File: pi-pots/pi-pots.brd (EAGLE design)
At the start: 40.6 x 101.6 mm, 5 parts, among them J1 PINHD-3X4

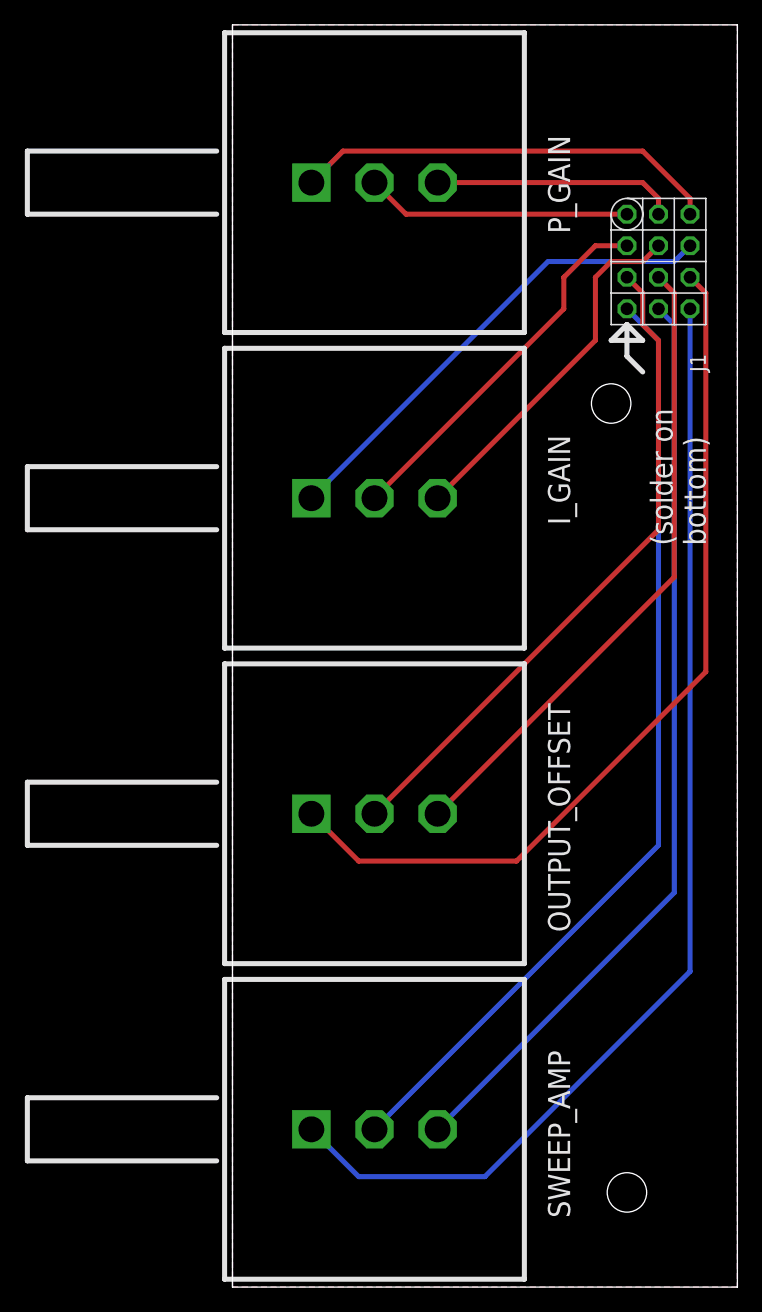
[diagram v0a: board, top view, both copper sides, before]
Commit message: Calibration Windows
I've opened up windows above POT1-3 and U9, pin 10. The windows allow access to the pots and U9 for initial calibration of the PI controller.

DSB
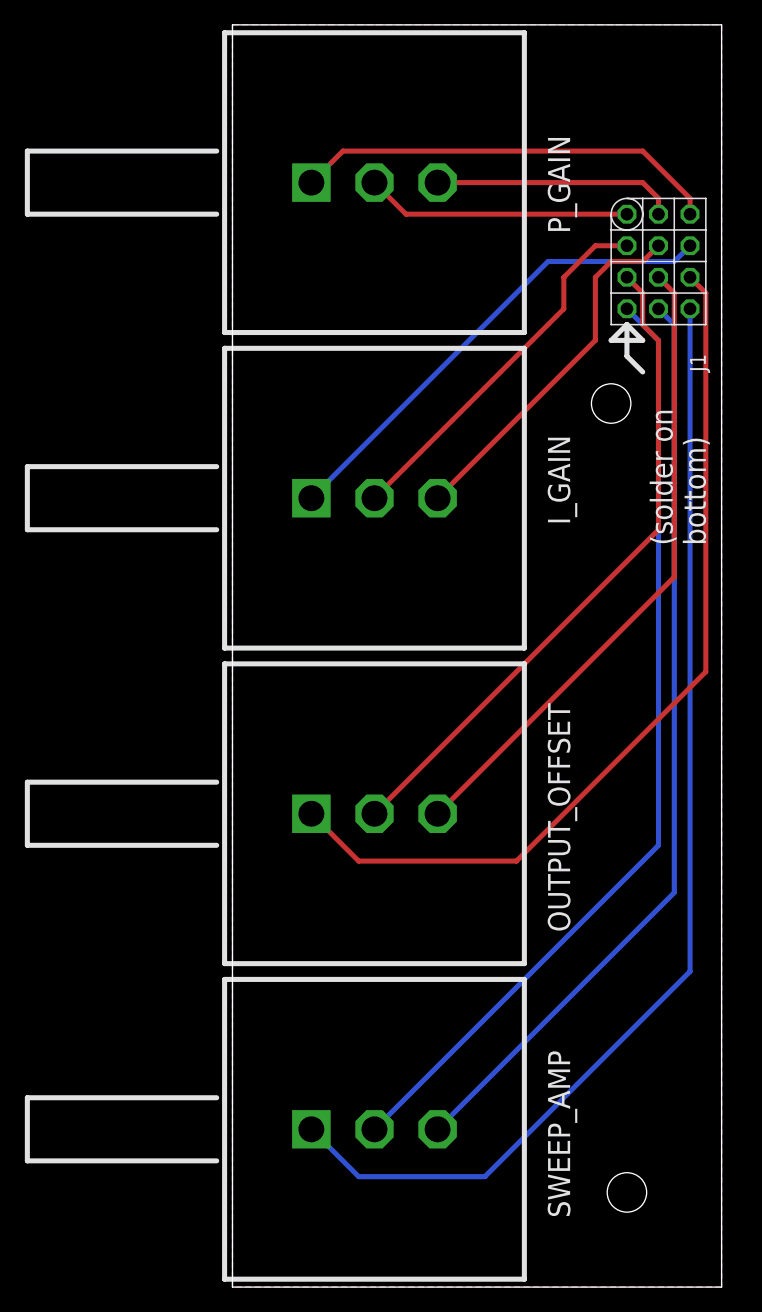
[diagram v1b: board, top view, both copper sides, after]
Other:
- board size 40.6 x 101.6 mm -> 39.4 x 101.6 mm
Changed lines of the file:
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@@
 <?xml version="1.0" encoding="utf-8"?>
 <!DOCTYPE eagle SYSTEM "eagle.dtd">
-<eagle version="6.6.0">
+<eagle version="9.3.0">
 <drawing>
 <settings>
-<setting alwaysvectorfont="yes"/>
+<setting alwaysvectorfont="no"/>
+<setting keepoldvectorfont="yes"/>
 <setting verticaltext="up"/>
 </settings>
-<grid distance="0.05" unitdist="inch" unit="inch" style="lines" multiple="1" display="yes" altdistance="0.025" altunitdist="inch" altunit="inch"/>
+<grid distance="0.01" unitdist="inch" unit="inch" style="lines" multiple="1" display="yes" altdistance="0.001" altunitdist="inch" altunit="inch"/>
 <layers>
 <layer number="1" name="Top" color="4" fill="1" visible="yes" active="yes"/>
@@
 <board>
 <plain>
-<wire x1="0" y1="101.6" x2="40.64" y2="101.6" width="0" layer="20"/>
-<wire x1="40.64" y1="101.6" x2="40.64" y2="0" width="0" layer="20"/>
-<wire x1="40.64" y1="0" x2="0" y2="0" width="0" layer="20"/>
+<wire x1="0" y1="101.6" x2="39.37" y2="101.6" width="0" layer="20"/>
+<wire x1="39.37" y1="101.6" x2="39.37" y2="0" width="0" layer="20"/>
+<wire x1="39.37" y1="0" x2="0" y2="0" width="0" layer="20"/>
 <wire x1="0" y1="0" x2="0" y2="101.6" width="0" layer="20"/>
 <hole x="30.48" y="71.12" drill="3.175"/>
@@
 </class>
 </classes>
-<designrules name="default">
-<description language="de">&lt;b&gt;EAGLE Design Rules&lt;/b&gt;
-&lt;p&gt;
-Die Standard-Design-Rules sind so gewählt, dass sie für
-die meisten Anwendungen passen. Sollte ihre Platine
-besondere Anforderungen haben, treffen Sie die erforderlichen
-Einstellungen hier und speichern die Design Rules unter
-einem neuen Namen ab.</description>
-<description language="en">&lt;b&gt;EAGLE Design Rules&lt;/b&gt;
-&lt;p&gt;
-The default Design Rules have been set to cover
-a wide range of applications. Your particular design
-may have different requirements, so please make the
-necessary adjustments and save your customized
-design rules under a new name.</description>
+<designrules name="MF_Standard_2_Layer">
+<description language="en">&lt;b&gt;MacroFab, INC. EAGLE Design Rules&lt;/b&gt;
+&lt;p&gt;This DRC check is for 2-Layer Standard Capability boards to be manufactured through the MacroFab, INC. service.</description>
 <param name="layerSetup" value="(1*16)"/>
-<param name="mtCopper" value="0.035mm 0.035mm 0.035mm 0.035mm 0.035mm 0.035mm 0.035mm 0.035mm 0.035mm 0.035mm 0.035mm 0.035mm 0.035mm 0.035mm 0.035mm 0.035mm"/>
-<param name="mtIsolate" value="1.5mm 0.15mm 0.2mm 0.15mm 0.2mm 0.15mm 0.2mm 0.15mm 0.2mm 0.15mm 0.2mm 0.15mm 0.2mm 0.15mm 0.2mm"/>
-<param name="mdWireWire" value="8mil"/>
-<param name="mdWirePad" value="8mil"/>
-<param name="mdWireVia" value="8mil"/>
-<param name="mdPadPad" value="8mil"/>
-<param name="mdPadVia" value="8mil"/>
-<param name="mdViaVia" value="8mil"/>
-<param name="mdSmdPad" value="8mil"/>
-<param name="mdSmdVia" value="8mil"/>
-<param name="mdSmdSmd" value="8mil"/>
+<param name="mtCopper" value="0.035mm 0.0175mm 0.035mm 0.035mm 0.035mm 0.035mm 0.035mm 0.035mm 0.035mm 0.035mm 0.035mm 0.035mm 0.035mm 0.035mm 0.0175mm 0.035mm"/>
+<param name="mtIsolate" value="1.5mm 1.1mm 0.2mm 0.15mm 0.2mm 0.15mm 0.2mm 0.15mm 0.2mm 0.15mm 0.2mm 0.15mm 0.2mm 0.15mm 0.2mm"/>
+<param name="mdWireWire" value="5mil"/>
+<param name="mdWirePad" value="5mil"/>
+<param name="mdWireVia" value="5mil"/>
+<param name="mdPadPad" value="5mil"/>
+<param name="mdPadVia" value="5mil"/>
+<param name="mdViaVia" value="5mil"/>
+<param name="mdSmdPad" value="0mil"/>
+<param name="mdSmdVia" value="0mil"/>
+<param name="mdSmdSmd" value="0mil"/>
 <param name="mdViaViaSameLayer" value="8mil"/>
 <param name="mnLayersViaInSmd" value="2"/>
-<param name="mdCopperDimension" value="40mil"/>
-<param name="mdDrill" value="8mil"/>
+<param name="mdCopperDimension" value="10mil"/>
+<param name="mdDrill" value="10mil"/>
 <param name="mdSmdStop" value="0mil"/>
-<param name="msWidth" value="10mil"/>
-<param name="msDrill" value="24mil"/>
-<param name="msMicroVia" value="9.99mm"/>
+<param name="msWidth" value="5mil"/>
+<param name="msDrill" value="10mil"/>
+<param name="msMicroVia" value="10mil"/>
 <param name="msBlindViaRatio" value="0.5"/>
 <param name="rvPadTop" value="0.25"/>
@@
 <param name="rvMicroViaOuter" value="0.25"/>
 <param name="rvMicroViaInner" value="0.25"/>
-<param name="rlMinPadTop" value="10mil"/>
+<param name="rlMinPadTop" value="4mil"/>
 <param name="rlMaxPadTop" value="20mil"/>
-<param name="rlMinPadInner" value="10mil"/>
+<param name="rlMinPadInner" value="4mil"/>
 <param name="rlMaxPadInner" value="20mil"/>
-<param name="rlMinPadBottom" value="10mil"/>
+<param name="rlMinPadBottom" value="4mil"/>
 <param name="rlMaxPadBottom" value="20mil"/>
-<param name="rlMinViaOuter" value="8mil"/>
+<param name="rlMinViaOuter" value="4mil"/>
 <param name="rlMaxViaOuter" value="20mil"/>
-<param name="rlMinViaInner" value="8mil"/>
+<param name="rlMinViaInner" value="4mil"/>
 <param name="rlMaxViaInner" value="20mil"/>
 <param name="rlMinMicroViaOuter" value="4mil"/>
@@
 <param name="psTop" value="-1"/>
 <param name="psBottom" value="-1"/>
-<param name="psFirst" value="-1"/>
+<param name="psFirst" value="0"/>
 <param name="psElongationLong" value="100"/>
 <param name="psElongationOffset" value="100"/>
 <param name="mvStopFrame" value="1"/>
 <param name="mvCreamFrame" value="0"/>
-<param name="mlMinStopFrame" value="4mil"/>
-<param name="mlMaxStopFrame" value="4mil"/>
+<param name="mlMinStopFrame" value="2mil"/>
+<param name="mlMaxStopFrame" value="2mil"/>
 <param name="mlMinCreamFrame" value="0mil"/>
 <param name="mlMaxCreamFrame" value="0mil"/>
-<param name="mlViaStopLimit" value="0mil"/>
+<param name="mlViaStopLimit" value="25mil"/>
 <param name="srRoundness" value="0"/>
 <param name="srMinRoundness" value="0mil"/>
@@
 <param name="dpMaxLengthDifference" value="10mm"/>
 <param name="dpGapFactor" value="2.5"/>
-<param name="checkGrid" value="0"/>
 <param name="checkAngle" value="0"/>
 <param name="checkFont" value="1"/>
-<param name="checkRestrict" value="1"/>
+<param name="checkRestrict" value="0"/>
+<param name="checkStop" value="0"/>
+<param name="checkValues" value="0"/>
+<param name="checkNames" value="1"/>
+<param name="checkWireStubs" value="1"/>
+<param name="checkPolygonWidth" value="0"/>
 <param name="useDiameter" value="13"/>
 <param name="maxErrors" value="50"/>
@@
 <pass name="Default">
 <param name="RoutingGrid" value="50mil"/>
+<param name="AutoGrid" value="1"/>
+<param name="Efforts" value="0"/>
+<param name="TopRouterVariant" value="1"/>
 <param name="tpViaShape" value="round"/>
 <param name="PrefDir.1" value="|"/>
@@
 <polygon width="0.4064" layer="16" isolate="1.27">
 <vertex x="0" y="101.6"/>
-<vertex x="40.64" y="101.6"/>
-<vertex x="40.64" y="0"/>
+<vertex x="39.37" y="101.6"/>
+<vertex x="39.37" y="0"/>
 <vertex x="0" y="0"/>
 </polygon>
@@
 <polygon width="0.4064" layer="1" isolate="1.27">
 <vertex x="0" y="101.6"/>
-<vertex x="40.64" y="101.6"/>
-<vertex x="40.64" y="0"/>
+<vertex x="39.37" y="101.6"/>
+<vertex x="39.37" y="0"/>
 <vertex x="0" y="0"/>
 </polygon>
 </signal>
 </signals>
+<mfgpreviewcolors>
+<mfgpreviewcolor name="soldermaskcolor" color="0xC8008000"/>
+<mfgpreviewcolor name="silkscreencolor" color="0xFFFEFEFE"/>
+<mfgpreviewcolor name="backgroundcolor" color="0xFF282828"/>
+<mfgpreviewcolor name="coppercolor" color="0xFFFFBF00"/>
+<mfgpreviewcolor name="substratecolor" color="0xFF786E46"/>
+</mfgpreviewcolors>
 </board>
 </drawing>
